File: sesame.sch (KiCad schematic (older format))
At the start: 153 parts, among them U1 ATmega32A-PU

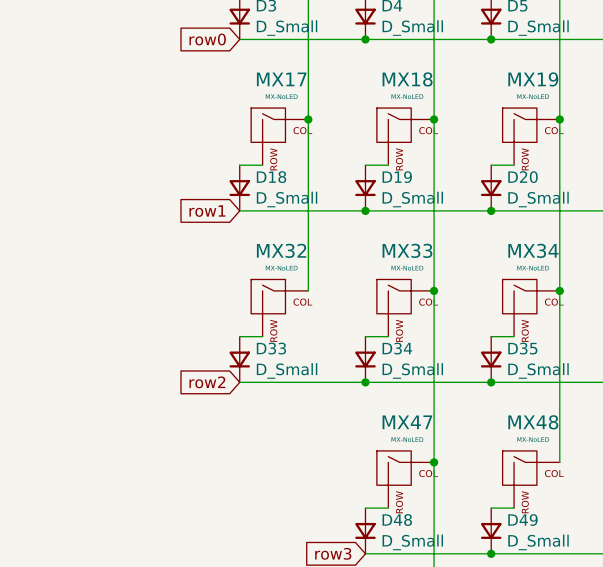
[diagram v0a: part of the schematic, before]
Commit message: add stepped caps support
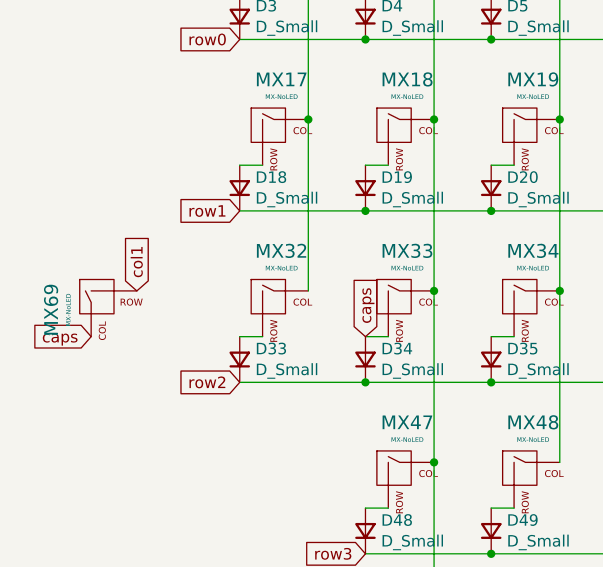
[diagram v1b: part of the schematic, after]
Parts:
- added MX69: MX-NoLED, MX_Only:MXOnly-1.25U-NoLED, symbol MX_Alps_Hybrid:MX-NoLED
- MX18: footprint MX_Only:MXOnly-1U-NoLED -> MX_Only:MXOnly-1.5U-NoLED
- MX33: footprint MX_Only:MXOnly-1U-NoLED -> MX_Only:MXOnly-1.75U-NoLED
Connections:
- net col1: now also MX69.2 (ROW)
- net caps: now reaches D34.2 (A), MX33.2 (ROW)
- net caps: now also MX69.1 (COL)
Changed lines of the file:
@@
 F 0 "MX18" H 2483 1873 60  0000 C CNN
 F 1 "MX-NoLED" H 2483 1799 20  0000 C CNN
-F 2 "MX_Only:MXOnly-1U-NoLED" H 1825 1625 60  0001 C CNN
+F 2 "MX_Only:MXOnly-1.5U-NoLED" H 1825 1625 60  0001 C CNN
 F 3 "" H 1825 1625 60  0001 C CNN
 	1    2450 1650
@@
 F 0 "MX33" H 2483 2623 60  0000 C CNN
 F 1 "MX-NoLED" H 2483 2549 20  0000 C CNN
-F 2 "MX_Only:MXOnly-1U-NoLED" H 1825 2375 60  0001 C CNN
+F 2 "MX_Only:MXOnly-1.75U-NoLED" H 1825 2375 60  0001 C CNN
 F 3 "" H 1825 2375 60  0001 C CNN
 	1    2450 2400
@@
 Text GLabel 2300 3500 0    50   Input ~ 0
 row3
+$Comp
+L MX_Alps_Hybrid:MX-NoLED MX69
+U 1 1 5F27D25B
+P 1150 2400
+F 0 "MX69" H 1183 2623 60  0000 C CNN
+F 1 "MX-NoLED" H 1183 2549 20  0000 C CNN
+F 2 "MX_Only:MXOnly-1.25U-NoLED" H 525 2375 60  0001 C CNN
+F 3 "" H 525 2375 60  0001 C CNN
+	1    1150 2400
+	0    -1   1    0
+$EndComp
+Text GLabel 1300 2350 1    50   Input ~ 0
+col1
+Text GLabel 2300 2550 1    50   Input ~ 0
+caps
+Text GLabel 1100 2550 0    50   Input ~ 0
+caps
 $EndSCHEMATC

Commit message: minor design changes
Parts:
- added AVR1: Conn_01x06, Connector_PinHeader_2.54mm:PinHeader_1x06_P2.54mm_Vertical, symbol Connector_Generic:Conn_01x06
- C1: footprint Capacitor_THT:CP_Radial_D5.0mm_P2.50mm -> Capacitor_THT:CP_Radial_D4.0mm_P1.50mm
- MX15: footprint MX_Only:MXOnly-2.25U-NoLED -> MX_Only:MXOnly-2U-NoLED
- MX31: footprint MX_Only:MXOnly-1U-NoLED -> MX_Only:MXOnly-1.5U-NoLED
- MX59: footprint MX_Only:MXOnly-1.5U-NoLED -> MX_Only:MXOnly-1.75U-NoLED
- MX61: footprint MX_Only:MXOnly-2.25U-NoLED -> MX_Only:MXOnly-2.75U-NoLED
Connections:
- net +5V: now also AVR1.6 (Pin_6)
- net GND: now also AVR1.1 (Pin_1)
- net MISO: now also AVR1.3 (Pin_3)
- net MOSI: now also AVR1.2 (Pin_2)
- net SCK: now also AVR1.4 (Pin_4)
- net reset: now also AVR1.5 (Pin_5)
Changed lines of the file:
@@
 F 0 "C1" H 3100 6850 50  0000 L CNN
 F 1 "4.7u" H 3100 6750 50  0000 L CNN
-F 2 "Capacitor_THT:CP_Radial_D5.0mm_P2.50mm" H 3000 6850 50  0001 C CNN
+F 2 "Capacitor_THT:CP_Radial_D4.0mm_P1.50mm" H 3000 6850 50  0001 C CNN
 F 3 "~" H 3000 6850 50  0001 C CNN
 	1    3000 6850
@@
 F 0 "MX15" H 9550 1100 60  0000 C CNN
 F 1 "MX-NoLED" H 9550 1050 20  0000 C CNN
-F 2 "MX_Only:MXOnly-2.25U-NoLED" H 8975 875 60  0001 C CNN
+F 2 "MX_Only:MXOnly-2U-NoLED" H 8975 875 60  0001 C CNN
 F 3 "" H 8975 875 60  0001 C CNN
 	1    9600 900
@@
 F 0 "MX31" H 9633 1873 60  0000 C CNN
 F 1 "MX-NoLED" H 9633 1799 20  0000 C CNN
-F 2 "MX_Only:MXOnly-1U-NoLED" H 8975 1625 60  0001 C CNN
+F 2 "MX_Only:MXOnly-1.5U-NoLED" H 8975 1625 60  0001 C CNN
 F 3 "" H 8975 1625 60  0001 C CNN
 	1    9600 1650
@@
 F 0 "MX59" H 9083 3373 60  0000 C CNN
 F 1 "MX-NoLED" H 9083 3299 20  0000 C CNN
-F 2 "MX_Only:MXOnly-1.5U-NoLED" H 8425 3125 60  0001 C CNN
+F 2 "MX_Only:MXOnly-1.75U-NoLED" H 8425 3125 60  0001 C CNN
 F 3 "" H 8425 3125 60  0001 C CNN
 	1    9050 3150
@@
 F 0 "MX61" H 10100 3350 60  0000 C CNN
 F 1 "MX-NoLED" H 10100 3300 20  0000 C CNN
-F 2 "MX_Only:MXOnly-2.25U-NoLED" H 9525 3125 60  0001 C CNN
+F 2 "MX_Only:MXOnly-2.75U-NoLED" H 9525 3125 60  0001 C CNN
 F 3 "" H 9525 3125 60  0001 C CNN
 	1    10150 3150
@@
 Text GLabel 1100 2550 0    50   Input ~ 0
 caps
+Text GLabel 5500 7200 2    50   Input ~ 0
+MOSI
+Text GLabel 5500 7100 2    50   Input ~ 0
+MISO
+Text GLabel 5500 7000 2    50   Input ~ 0
+SCK
+$Comp
+L power:GND #PWR0101
+U 1 1 5F329387
+P 5750 7300
+F 0 "#PWR0101" H 5750 7050 50  0001 C CNN
+F 1 "GND" H 5755 7127 50  0000 C CNN
+F 2 "" H 5750 7300 50  0001 C CNN
+F 3 "" H 5750 7300 50  0001 C CNN
+	1    5750 7300
+	1    0    0    -1
+$EndComp
+$Comp
+L power:+5V #PWR0102
+U 1 1 5F329944
+P 5750 6800
+F 0 "#PWR0102" H 5750 6650 50  0001 C CNN
+F 1 "+5V" H 5765 6973 50  0000 C CNN
+F 2 "" H 5750 6800 50  0001 C CNN
+F 3 "" H 5750 6800 50  0001 C CNN
+	1    5750 6800
+	1    0    0    -1
+$EndComp
+Text GLabel 5500 6900 2    50   Input ~ 0
+reset
+$Comp
+L Connector_Generic:Conn_01x06 AVR1
+U 1 1 5F32D9BD
+P 5300 7100
+F 0 "AVR1" H 5218 6575 50  0000 C CNN
+F 1 "Conn_01x06" H 5218 6666 50  0000 C CNN
+F 2 "Connector_PinHeader_2.54mm:PinHeader_1x06_P2.54mm_Vertical" H 5300 7100 50  0001 C CNN
+F 3 "~" H 5300 7100 50  0001 C CNN
+	1    5300 7100
+	-1   0    0    1
+$EndComp
+Wire Wire Line
+	5500 7300 5750 7300
+Wire Wire Line
+	5500 6800 5750 6800
 $EndSCHEMATC

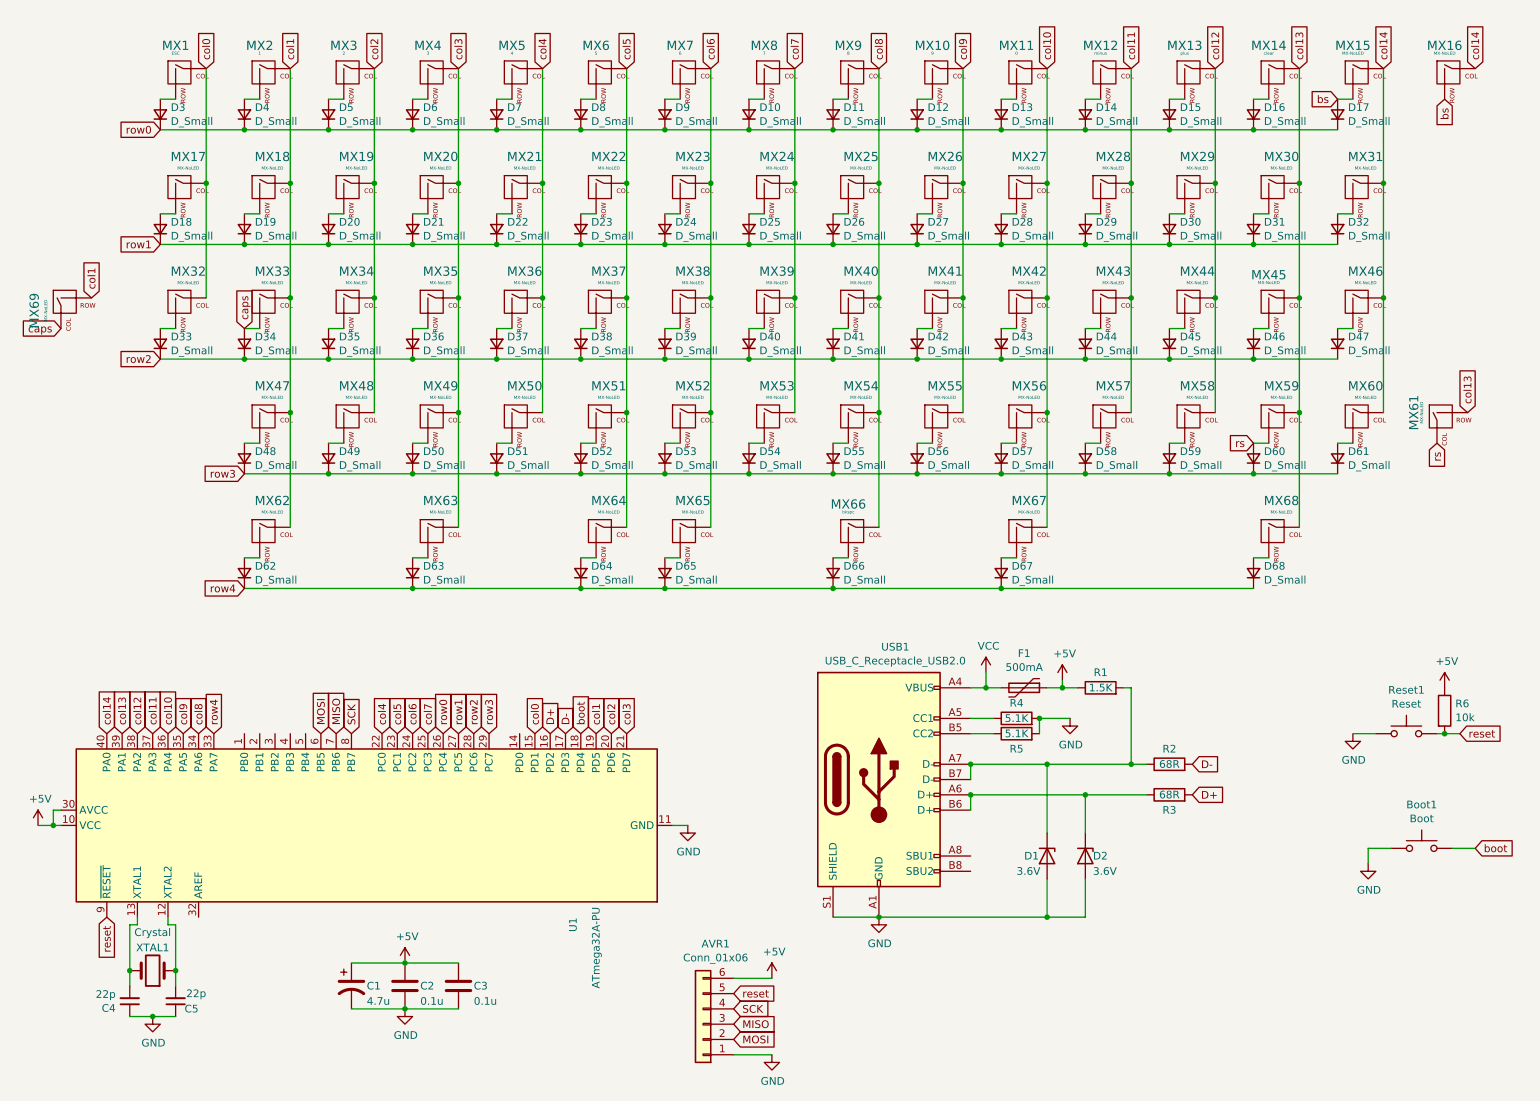
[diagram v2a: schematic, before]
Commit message: fix routing error
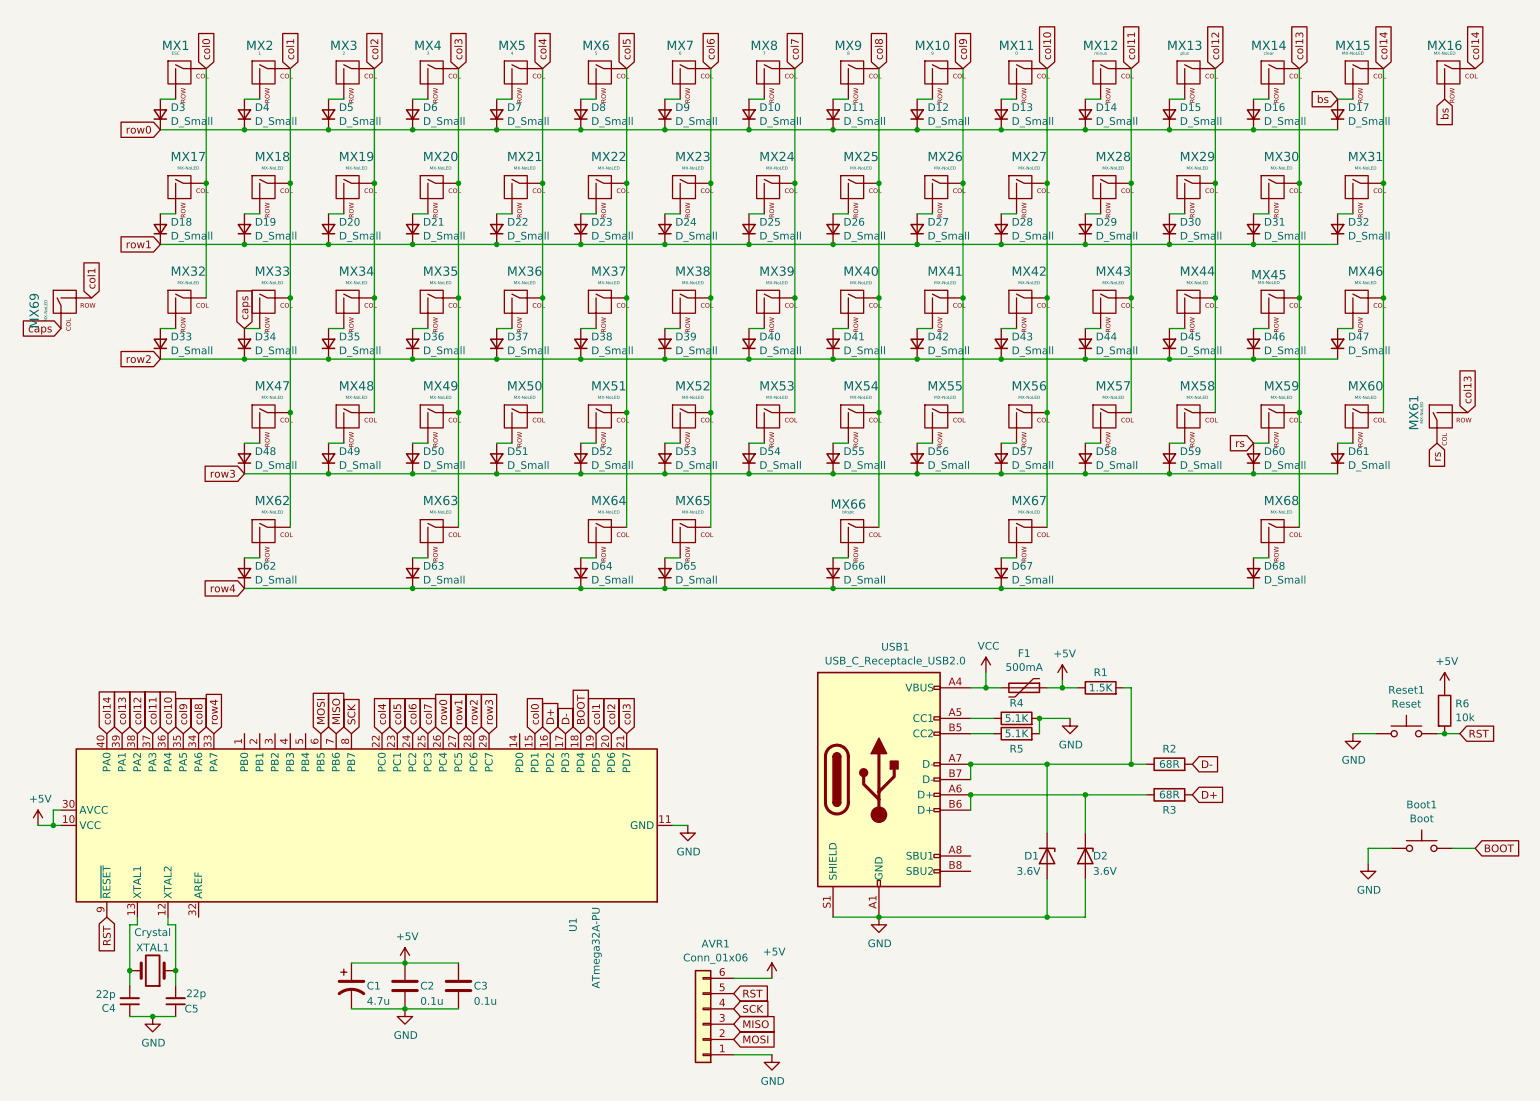
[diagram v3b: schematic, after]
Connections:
- net boot renamed BOOT
- net reset renamed RST
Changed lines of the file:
@@
 $EndComp
 Text GLabel 1400 6400 3    50   Input ~ 0
-reset
+RST
 Text GLabel 10250 5200 2    50   Input ~ 0
-reset
+RST
 $Comp
 L power:GND #PWR05
@@
 	1    0    0    -1
 $EndComp
-Text GLabel 10350 5950 2    50   Input ~ 0
-boot
 Wire Wire Line
 	10350 5950 10200 5950
@@
 $EndComp
 Text GLabel 4500 5200 1    50   Input ~ 0
-boot
+BOOT
 Text GLabel 4300 5200 1    50   Input ~ 0
 D+
@@
 $EndComp
 Text GLabel 5500 6900 2    50   Input ~ 0
-reset
+RST
 $Comp
 L Connector_Generic:Conn_01x06 AVR1
@@
 Wire Wire Line
 	5500 6800 5750 6800
+Text GLabel 10350 5950 2    50   Input ~ 0
+BOOT
 $EndSCHEMATC

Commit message: add 2.25u left space support and update caps to use cftkb footprints
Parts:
- added MX70: MX-NoLED, MX_Only:MXOnly-2.25U-ReversedStabilizers-NoLED, symbol MX_Alps_Hybrid:MX-NoLED
- added MX71: MX-NoLED, MX_Only:MXOnly-1U-NoLED, symbol MX_Alps_Hybrid:MX-NoLED
- MX62, MX63: footprint MX_Only:MXOnly-1U-NoLED -> MX_Only:MXOnly-1.5U-NoLED
- USB1: symbol Connector:USB_C_Receptacle_USB2.0 -> sesame-rescue:USB_C_Receptacle_USB2.0-Connector
- renumbered R3 to R2, R2 to R3
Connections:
- net col5: now also MX70.1 (COL)
- net col6: now also MX71.1 (COL)
- net at D64.2 (A), MX64.2 (ROW): now also MX70.2 (ROW)
- net at D65.2 (A), MX65.2 (ROW): now also MX71.2 (ROW)
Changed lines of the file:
@@
 D-
 $Comp
-L Device:R R3
+L Device:R R2
 U 1 1 5EC46F28
 P 8350 5600
-F 0 "R3" V 8250 5600 50  0000 C CNN
+F 0 "R2" V 8250 5600 50  0000 C CNN
 F 1 "68R" V 8350 5600 50  0000 C CNN
 F 2 "Resistor_THT:R_Axial_DIN0207_L6.3mm_D2.5mm_P10.16mm_Horizontal" V 8280 5600 50  0001 C CNN
@@
 $EndComp
 $Comp
-L Device:R R2
+L Device:R R3
 U 1 1 5EC4799A
 P 8350 5400
-F 0 "R2" V 8450 5400 50  0000 C CNN
+F 0 "R3" V 8450 5400 50  0000 C CNN
 F 1 "68R" V 8350 5400 50  0000 C CNN
 F 2 "Resistor_THT:R_Axial_DIN0207_L6.3mm_D2.5mm_P10.16mm_Horizontal" V 8280 5400 50  0001 C CNN
@@
 F 0 "MX62" H 2483 4123 60  0000 C CNN
 F 1 "MX-NoLED" H 2483 4049 20  0000 C CNN
-F 2 "MX_Only:MXOnly-1U-NoLED" H 1825 3875 60  0001 C CNN
+F 2 "MX_Only:MXOnly-1.5U-NoLED" H 1825 3875 60  0001 C CNN
 F 3 "" H 1825 3875 60  0001 C CNN
 	1    2450 3900
@@
 F 0 "MX63" H 3583 4123 60  0000 C CNN
 F 1 "MX-NoLED" H 3583 4049 20  0000 C CNN
-F 2 "MX_Only:MXOnly-1U-NoLED" H 2925 3875 60  0001 C CNN
+F 2 "MX_Only:MXOnly-1.5U-NoLED" H 2925 3875 60  0001 C CNN
 F 3 "" H 2925 3875 60  0001 C CNN
 	1    3550 3900
@@
 	4500 4050 4600 4050
 Wire Wire Line
-	4800 3100 4800 3850
+	4800 3100 4800 3750
 $Comp
 L MX_Alps_Hybrid:MX-NoLED MX65
@@
 	5050 4050 5150 4050
 Wire Wire Line
-	5350 3100 5350 3850
+	5350 3100 5350 3750
 Connection ~ 4500 4250
 Wire Wire Line
@@
 	10150 5200 10250 5200
 $Comp
-L Connector:USB_C_Receptacle_USB2.0 USB1
+L sesame-rescue:USB_C_Receptacle_USB2.0-Connector USB1
 U 1 1 5F2A909F
 P 6450 5500
@@
 Text GLabel 10350 5950 2    50   Input ~ 0
 BOOT
+$Comp
+L MX_Alps_Hybrid:MX-NoLED MX70
+U 1 1 607BD789
+P 4550 3800
+F 0 "MX70" H 4583 4023 60  0000 C CNN
+F 1 "MX-NoLED" H 4583 3949 20  0000 C CNN
+F 2 "MX_Only:MXOnly-2.25U-ReversedStabilizers-NoLED" H 3925 3775 60  0001 C CNN
+F 3 "" H 3925 3775 60  0001 C CNN
+	1    4550 3800
+	1    0    0    -1
+$EndComp
+Wire Wire Line
+	4500 3950 4500 4050
+Connection ~ 4500 4050
+Wire Wire Line
+	4700 3750 4800 3750
+Connection ~ 4800 3750
+Wire Wire Line
+	4800 3750 4800 3850
+$Comp
+L MX_Alps_Hybrid:MX-NoLED MX71
+U 1 1 607DF981
+P 5100 3800
+F 0 "MX71" H 5133 4023 60  0000 C CNN
+F 1 "MX-NoLED" H 5133 3949 20  0000 C CNN
+F 2 "MX_Only:MXOnly-1U-NoLED" H 4475 3775 60  0001 C CNN
+F 3 "" H 4475 3775 60  0001 C CNN
+	1    5100 3800
+	1    0    0    -1
+$EndComp
+Wire Wire Line
+	5250 3750 5350 3750
+Connection ~ 5350 3750
+Wire Wire Line
+	5350 3750 5350 3850
+Wire Wire Line
+	5050 3950 5050 4050
+Connection ~ 5050 4050
 $EndSCHEMATC

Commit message: fixes
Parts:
- C2, C3: footprint Capacitor_THT:C_Disc_D3.0mm_W2.0mm_P2.50mm -> Capacitor_THT:C_Disc_D5.0mm_W2.5mm_P5.00mm
- C4, C5: footprint Capacitor_THT:C_Disc_D6.0mm_W2.5mm_P5.00mm -> Capacitor_THT:C_Disc_D5.0mm_W2.5mm_P2.50mm
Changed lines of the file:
@@
 F 0 "C2" H 3450 6850 50  0000 L CNN
 F 1 "0.1u" H 3450 6750 50  0000 L CNN
-F 2 "Capacitor_THT:C_Disc_D3.0mm_W2.0mm_P2.50mm" H 3388 6700 50  0001 C CNN
+F 2 "Capacitor_THT:C_Disc_D5.0mm_W2.5mm_P5.00mm" H 3388 6700 50  0001 C CNN
 F 3 "~" H 3350 6850 50  0001 C CNN
 	1    3350 6850
@@
 F 0 "C3" H 3800 6850 50  0000 L CNN
 F 1 "0.1u" H 3800 6750 50  0000 L CNN
-F 2 "Capacitor_THT:C_Disc_D3.0mm_W2.0mm_P2.50mm" H 3738 6700 50  0001 C CNN
+F 2 "Capacitor_THT:C_Disc_D5.0mm_W2.5mm_P5.00mm" H 3738 6700 50  0001 C CNN
 F 3 "~" H 3700 6850 50  0001 C CNN
 	1    3700 6850
@@
 F 0 "C5" H 1700 7000 50  0000 L CNN
 F 1 "22p" H 1650 6900 50  0000 L CNN
-F 2 "Capacitor_THT:C_Disc_D6.0mm_W2.5mm_P5.00mm" H 1850 6950 50  0001 C CNN
+F 2 "Capacitor_THT:C_Disc_D5.0mm_W2.5mm_P2.50mm" H 1850 6950 50  0001 C CNN
 F 3 "~" H 1850 6950 50  0001 C CNN
 	1    1850 6950
@@
 F 0 "C4" H 1642 6996 50  0000 L CNN
 F 1 "22p" H 1642 6905 50  0000 L CNN
-F 2 "Capacitor_THT:C_Disc_D6.0mm_W2.5mm_P5.00mm" H 1550 6950 50  0001 C CNN
+F 2 "Capacitor_THT:C_Disc_D5.0mm_W2.5mm_P2.50mm" H 1550 6950 50  0001 C CNN
 F 3 "~" H 1550 6950 50  0001 C CNN
 	1    1550 6950
